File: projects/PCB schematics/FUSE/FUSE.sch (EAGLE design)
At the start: 111 parts, among them J1 178328-2, J2 178328-2, J3 178328-2, J4 178328-2, J5 178328-2, J6 178328-2, J7 178328-2, J8 178328-2, J9 178328-2, X1 5566-20, X10 5566-20, X11 5566-20, X2 5566-20, X3 5566-20, X4 5566-20, X5 5566-20, X6 5566-20, X7 5566-20, X8 5566-20, X9 D1200D-20

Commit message: FUSE - Initial draft.
Squash - Highly Irrelevant update
Reason for commit: Couldn't figure out how to squash minor update into a big one.

Squash - FUSE - Initial draft done.

Board has been made for 24 fused connections. 4 of these will be needed, but the design can be repeated.

Silkscreen is the only thing to be edited.

Squash - FUSE - Minor tweaks.
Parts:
- removed F25, F26, F27, F28, F29, F30, F31, F32, F33, F34, F35, F36, F37, F38, F39, F40, F41, F42, F43, F44, F45, F46, F47, F48, F49, F50, F51, F52, F53, F54, F55, F56, F57, F58, F59, F60, F61, F62, F63, F64, F65, F66, F67, F68, F69, F70, F71, F72, F73, F74, F75, F76, F77, F78, F79, F80, F81, F82, F83, F84, F85, F86, F87, F88, F89, F90, F91: 0885001.DR, 0885001.DR:0885001.DR
- removed J3, J4, J5, J6, J7, J8, J9: 178328-2, 178328-2:178328-2
- removed X1, X10, X11, X2, X3, X4, X5, X6, X7, X8: 5566-20, con-molex:5566-20
- removed X9: D1200D-20, con-tyco:D1200D-20
- J1, J2: value 178328-2 -> 24P(90DEG)_1-794108-0; device 178328-2:178328-2 -> con-MATE-N-LOK:24P(90DEG)_1-794108-0
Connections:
- removed net INPUT25: F45.1, J3.A9, X3-5.S
- removed net INPUT26: F46.1, J3.B1, X3-6.S
- removed net INPUT27: F47.1, J3.B3, X3-7.S
- removed net INPUT28: F48.1, J3.B5, X3-8.S
- removed net INPUT29: F49.1, J3.B7, X3-9.S
- removed net INPUT30: F50.1, J3.B9, X3-10.S
- removed net INPUT31: F11.1, J4.A1, X3-11.S
- removed net INPUT32: F12.1, J4.A3, X3-12.S
- removed net INPUT33: F13.1, J4.A5, X3-13.S
- removed net INPUT34: F14.1, J4.A7, X3-14.S
- removed net INPUT35: F15.1, J4.A9, X3-15.S
- removed net INPUT36: F16.1, J4.B1, X3-16.S
- removed net INPUT37: F17.1, J4.B3, X3-17.S
- removed net INPUT38: F18.1, J4.B5, X3-18.S
- removed net INPUT39: F19.1, J4.B7, X3-19.S
- removed net INPUT40: F20.1, J4.B9, X3-20.S
- removed net INPUT41: F31.1, J5.A1, X4-1.S
- removed net INPUT42: F32.1, J5.A3, X4-2.S
- removed net INPUT43: F33.1, J5.A5, X4-3.S
- removed net INPUT44: F34.1, J5.A7, X4-4.S
- removed net INPUT45: F35.1, J5.A9, X4-5.S
- removed net INPUT46: F36.1, J5.B1, X4-6.S
- removed net INPUT47: F37.1, J5.B3, X4-7.S
- removed net INPUT48: F38.1, J5.B5, X4-8.S
- removed net INPUT49: F39.1, J5.B7, X4-9.S
- removed net INPUT50: F40.1, J5.B9, X4-10.S
- removed net INPUT51: F51.1, J6.A1, X4-11.S
- removed net INPUT52: F52.1, J6.A3, X4-12.S
- removed net INPUT53: F53.1, J6.A5, X4-13.S
- removed net INPUT54: F54.1, J6.A7, X4-14.S
- removed net INPUT55: F55.1, J6.A9, X4-15.S
- removed net INPUT56: F56.1, J6.B1, X4-16.S
- removed net INPUT57: F57.1, J6.B3, X4-17.S
- removed net INPUT58: F58.1, J6.B5, X4-18.S
- removed net INPUT59: F59.1, J6.B7, X4-19.S
- removed net INPUT60: F60.1, J6.B9, X4-20.S
- removed net INPUT61: F61.1, J7.A1, X5-1.S
- removed net INPUT62: F62.1, J7.A3, X5-2.S
- removed net INPUT63: F63.1, J7.A5, X5-3.S
- removed net INPUT64: F64.1, J7.A7, X5-4.S
- removed net INPUT65: F65.1, J7.A9, X5-5.S
- removed net INPUT66: F66.1, J7.B1, X5-6.S
- removed net INPUT67: F67.1, J7.B3, X5-7.S
- removed net INPUT68: F68.1, J7.B5, X5-8.S
- removed net INPUT69: F69.1, J7.B7, X5-9.S
- removed net INPUT70: F70.1, J7.B9, X5-10.S
- removed net INPUT71: F71.1, J8.A1, X5-11.S
- removed net INPUT72: F72.1, J8.A3, X5-12.S
- removed net INPUT73: F73.1, J8.A5, X5-13.S
- removed net INPUT74: F74.1, J8.A7, X5-14.S
- removed net INPUT75: F75.1, J8.A9, X5-15.S
- removed net INPUT76: F76.1, J8.B1, X5-16.S
- removed net INPUT77: F77.1, J8.B3, X5-17.S
- removed net INPUT78: F78.1, J8.B5, X5-18.S
- removed net INPUT79: F79.1, J8.B7, X5-19.S
- removed net INPUT80: F80.1, J8.B9, X5-20.S
- removed net INPUT81: F81.1, J9.A1, X10-1.S
- removed net INPUT82: F82.1, J9.A3, X10-2.S
- removed net INPUT83: F83.1, J9.A5, X10-3.S
- removed net INPUT84: F84.1, J9.A7, X10-4.S
- removed net INPUT85: F85.1, J9.A9, X10-5.S
- removed net INPUT86: F86.1, J9.B1, X10-6.S
- removed net INPUT87: F87.1, J9.B3, X10-7.S
- removed net INPUT88: F88.1, J9.B5, X10-8.S
- removed net INPUT89: F89.1, J9.B7, X10-9.S
- removed net INPUT90: F90.1, J9.B9, X10-10.S
- removed net INPUT91: F91.1, X10-11.S
- removed net OUTPUT25: F45.2, X6-5.S
- removed net OUTPUT26: F46.2, X6-6.S
- removed net OUTPUT27: F47.2, X6-7.S
- removed net OUTPUT28: F48.2, X6-8.S
- removed net OUTPUT29: F49.2, X6-9.S
- removed net OUTPUT30: F50.2, X6-10.S
- removed net OUTPUT31: F11.2, X6-11.S
- removed net OUTPUT32: F12.2, X6-12.S
- removed net OUTPUT33: F13.2, X6-13.S
- removed net OUTPUT34: F14.2, X6-14.S
- removed net OUTPUT35: F15.2, X6-15.S
- removed net OUTPUT36: F16.2, X6-16.S
- removed net OUTPUT37: F17.2, X6-17.S
- removed net OUTPUT38: F18.2, X6-18.S
- removed net OUTPUT39: F19.2, X6-19.S
- removed net OUTPUT40: F20.2, X6-20.S
- removed net OUTPUT41: F31.2, F61.2, X7-1.S
- removed net OUTPUT42: F32.2, X7-2.S
- removed net OUTPUT43: F33.2, X7-3.S
- removed net OUTPUT44: F34.2, X7-4.S
- removed net OUTPUT45: F35.2, X7-5.S
- removed net OUTPUT46: F36.2, X7-6.S
- removed net OUTPUT47: F37.2, X7-7.S
- removed net OUTPUT48: F38.2, X7-8.S
- removed net OUTPUT49: F39.2, X7-9.S
- removed net OUTPUT50: F40.2, X7-10.S
- removed net OUTPUT51: F51.2, X7-11.S
- removed net OUTPUT52: F52.2, X7-12.S
- removed net OUTPUT53: F53.2, X7-13.S
- removed net OUTPUT54: F54.2, X7-14.S
- removed net OUTPUT55: F55.2, X7-15.S
- removed net OUTPUT56: F56.2, X7-16.S
- removed net OUTPUT57: F57.2, X7-17.S
- removed net OUTPUT58: F58.2, X7-18.S
- removed net OUTPUT59: F59.2, X7-19.S
- removed net OUTPUT60: F60.2, X7-20.S
- removed net OUTPUT61: X8-1.S
- removed net OUTPUT62: F62.2, X8-2.S
- removed net OUTPUT63: F63.2, X8-3.S
- removed net OUTPUT64: F64.2, X8-4.S
- removed net OUTPUT65: F65.2, X8-5.S
- removed net OUTPUT66: F66.2, X8-6.S
- removed net OUTPUT67: F67.2, X8-7.S
- removed net OUTPUT68: F68.2, X8-8.S
- removed net OUTPUT69: F69.2, X8-9.S
- removed net OUTPUT70: F70.2, X8-10.S
- removed net OUTPUT71: F71.2, X8-11.S
- removed net OUTPUT72: F72.2, X8-12.S
- removed net OUTPUT73: F73.2, X8-13.S
- removed net OUTPUT74: F74.2, X8-14.S
- removed net OUTPUT75: F75.2, X8-15.S
- removed net OUTPUT76: F76.2, X8-16.S
- removed net OUTPUT77: F77.2, X8-17.S
- removed net OUTPUT78: F78.2, X8-18.S
- removed net OUTPUT79: F79.2, X8-19.S
- removed net OUTPUT80: F80.2, X8-20.S
- removed net OUTPUT81: F81.2, X11-1.S
- removed net OUTPUT82: F82.2, X11-2.S
- removed net OUTPUT83: F83.2, X11-3.S
- removed net OUTPUT84: F84.2, X11-4.S
- removed net OUTPUT85: F85.2, X11-5.S
- removed net OUTPUT86: F86.2, X11-6.S
- removed net OUTPUT87: F87.2, X11-7.S
- removed net OUTPUT88: F88.2, X11-8.S
- removed net OUTPUT89: F89.2, X11-9.S
- removed net OUTPUT90: F90.2, X11-10.S
- removed net OUTPUT91: F91.2, X11-11.S
- removed net OUTPUT\4: F4.2
- net INPUT1: now also J1.1; no longer J1.A1, X1-1.S
- net INPUT10: now also J1.10; no longer J1.B9, X1-10.S
- net INPUT11: now also F11.1, J1.11; no longer F21.1, J2.A1, X1-11.S
- net INPUT12: now also F12.1, J1.12; no longer F22.1, J2.A3, X1-12.S
- net INPUT13: now also F13.1, J1.13; no longer F23.1, J2.A5, X1-13.S
- net INPUT14: now also F14.1, J1.14; no longer F24.1, J2.A7, X1-14.S
- net INPUT15: now also F15.1, J1.15; no longer F25.1, J2.A9, X1-15.S
- net INPUT16: now also F16.1, J1.16; no longer F26.1, J2.B1, X1-16.S
- net INPUT17: now also F17.1, J1.17; no longer F27.1, J2.B3, X1-17.S
- net INPUT18: now also F18.1, J1.18; no longer F28.1, J2.B5, X1-18.S
- net INPUT19: now also F19.1, J1.19; no longer F29.1, J2.B7, X1-19.S
- net INPUT2: now also J1.2; no longer J1.A3, X1-2.S
- net INPUT20: now also F20.1, J1.20; no longer F30.1, J2.B9, X1-20.S
- net INPUT21: now also F21.1, J1.21; no longer F41.1, J3.A1, X3-1.S
- net INPUT22: now also F22.1, J1.22; no longer F42.1, J3.A3, X3-2.S
- net INPUT23: now also F23.1, J1.23; no longer F43.1, J3.A5, X3-3.S
- net INPUT24: now also F24.1, J1.24; no longer F44.1, J3.A7, X3-4.S
- net INPUT3: now also J1.3; no longer J1.A5, X1-3.S
- net INPUT4: now also J1.4; no longer J1.A7, X1-4.S
- net INPUT5: now also J1.5; no longer J1.A9, X1-5.S
- net INPUT6: now also J1.6; no longer J1.B1, X1-6.S
- net INPUT7: now also J1.7; no longer J1.B3, X1-7.S
- net INPUT8: now also J1.8; no longer J1.B5, X1-8.S
- net INPUT9: now also J1.9; no longer J1.B7, X1-9.S
- net OUTPUT1: now also J2.1; no longer X2-1.S
- net OUTPUT10: now also J2.10; no longer X2-10.S
- net OUTPUT11: now also F11.2, J2.11; no longer F21.2, X2-11.S
- net OUTPUT12: now also F12.2, J2.12; no longer F22.2, X2-12.S
- net OUTPUT13: now also F13.2, J2.13; no longer F23.2, X2-13.S
- net OUTPUT14: now also F14.2, J2.14; no longer F24.2, X2-14.S
- net OUTPUT15: now also F15.2, J2.15; no longer F25.2, X2-15.S
- net OUTPUT16: now also F16.2, J2.16; no longer F26.2, X2-16.S
- net OUTPUT17: now also F17.2, J2.17; no longer F27.2, X2-17.S
- net OUTPUT18: now also F18.2, J2.18; no longer F28.2, X2-18.S
- net OUTPUT19: now also F19.2, J2.19; no longer F29.2, X2-19.S
- net OUTPUT2: now also J2.2; no longer X2-2.S
- net OUTPUT20: now also F20.2, J2.20; no longer F30.2, X2-20.S
- net OUTPUT21: now also F21.2, J2.21; no longer F41.2, X6-1.S
- net OUTPUT22: now also F22.2, J2.22; no longer F42.2, X6-2.S
- net OUTPUT23: now also F23.2, J2.23; no longer F43.2, X6-3.S
- net OUTPUT24: now also F24.2, J2.24; no longer F44.2, X6-4.S
- net OUTPUT3: now also J2.3; no longer X2-3.S
- net OUTPUT4: now also F4.2, J2.4; no longer X2-4.S
- net OUTPUT5: now also J2.5; no longer X2-5.S
- net OUTPUT6: now also J2.6; no longer X2-6.S
- net OUTPUT7: now also J2.7; no longer X2-7.S
- net OUTPUT8: now also J2.8; no longer X2-8.S
- net OUTPUT9: now also J2.9; no longer X2-9.S
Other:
- moved on the sheet: F1, F10, F11, F12, F13, F14, F15, F16, F17, F18, F19, F2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

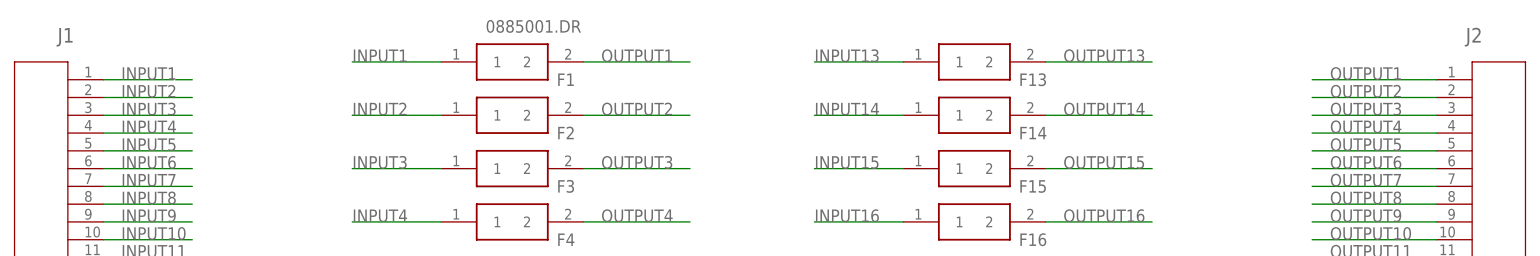
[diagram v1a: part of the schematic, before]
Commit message: PROJ - Silkscreen modifications - 50%.
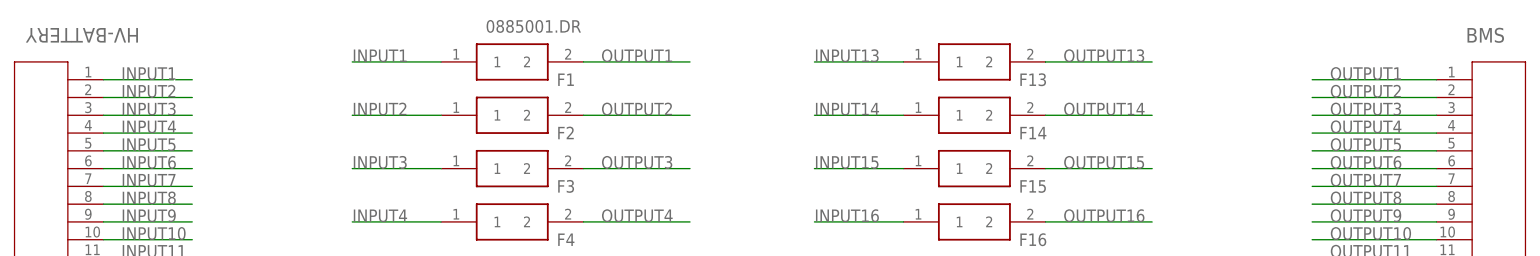
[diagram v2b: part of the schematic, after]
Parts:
- renumbered J1 to HV-BATTERY, J2 to BMS

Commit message: PROJ - Gerber files major milestone - 05/05/19.
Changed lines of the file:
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@@
 <segment>
 <label x="20.32" y="91.44" size="1.778" layer="95"/>
-<wire x1="27.7876" y1="91.44" x2="17.78" y2="91.44" width="0.1524" layer="91"/>
+<wire x1="30.5816" y1="91.44" x2="17.78" y2="91.44" width="0.1524" layer="91"/>
 <pinref part="HV-BATTERY" gate="A" pin="1"/>
 </segment>
@@
 </segment>
 </net>
-<net name="N$48" class="0">
-<segment>
-<wire x1="30.48" y1="91.44" x2="28.0924" y2="91.44" width="0.1524" layer="91"/>
-</segment>
-</net>
